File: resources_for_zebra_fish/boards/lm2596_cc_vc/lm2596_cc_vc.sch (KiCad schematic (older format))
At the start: 26 parts, among them J1 Vin, J2 Conn_Coaxial, J3 external_on/off, J4 to_mosfet, J5 red_vout, U1 LM2596T-3.3, U2 LM2596T-ADJ, U3 MCP602

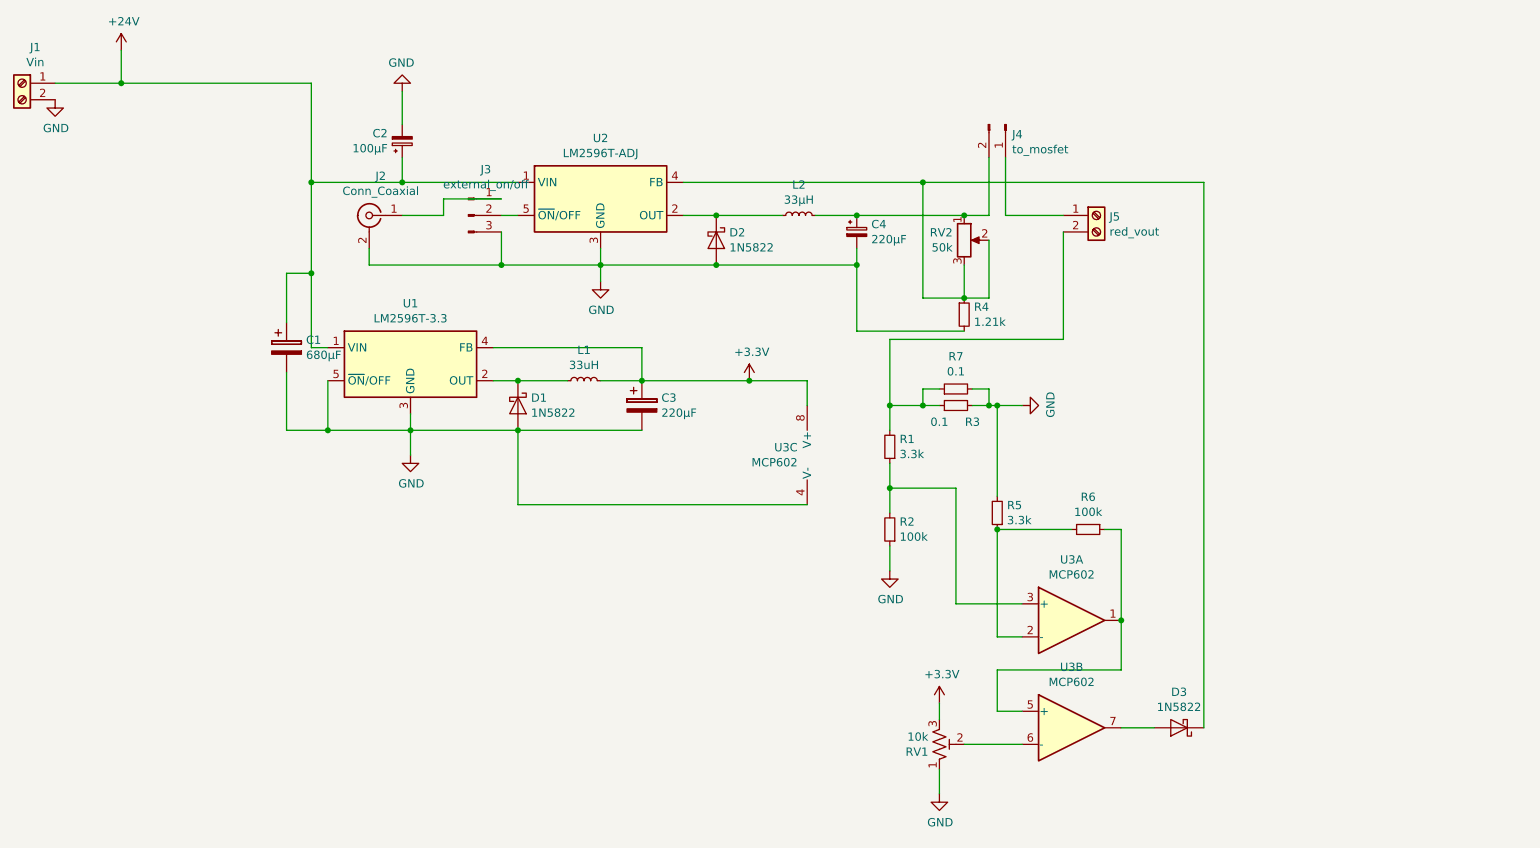
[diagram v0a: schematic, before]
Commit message: new board: power supply and sync to led in one
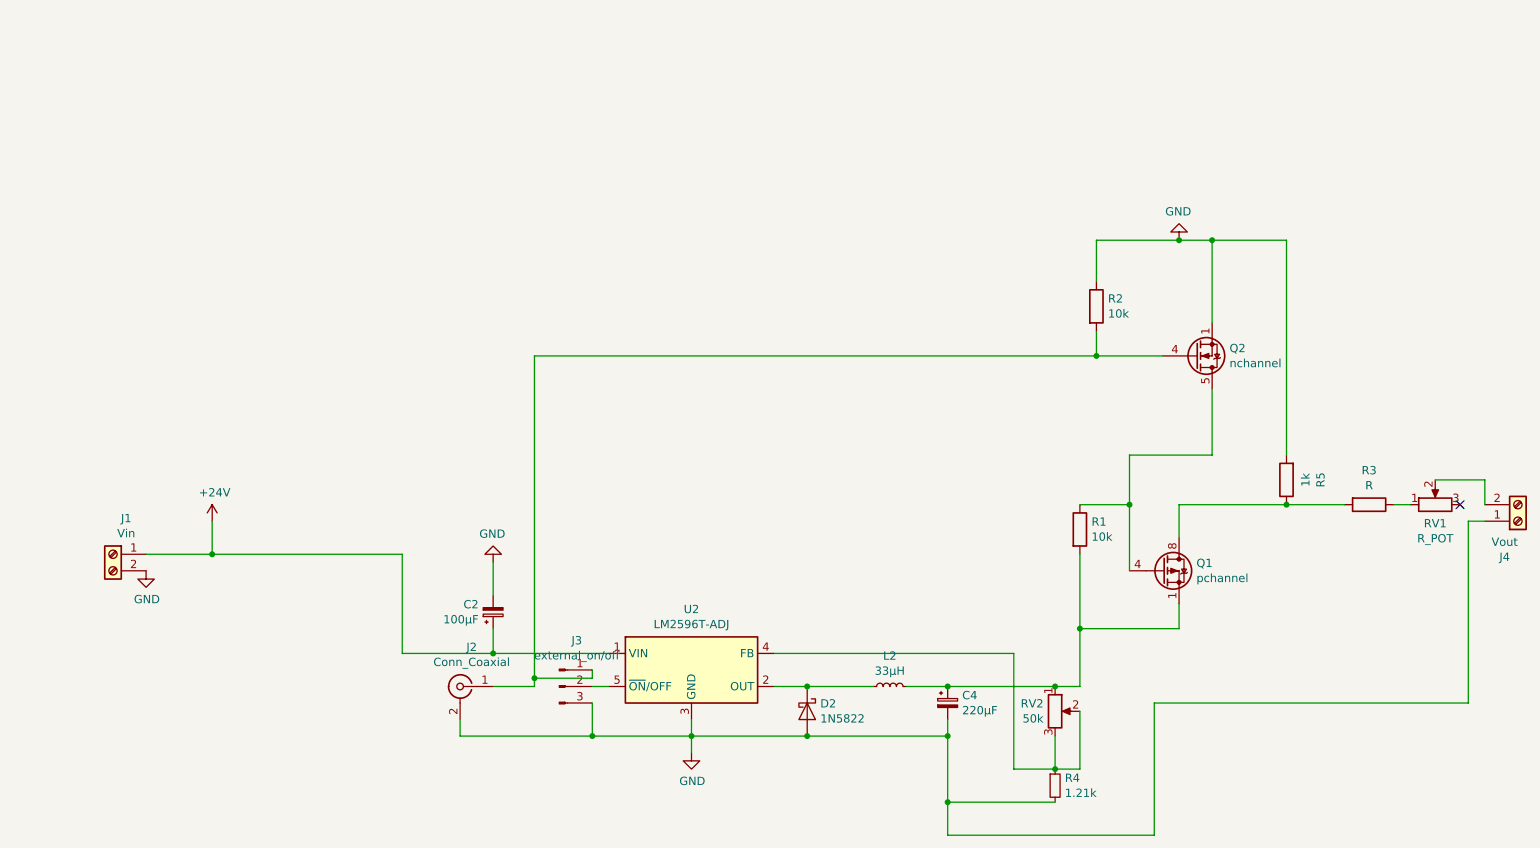
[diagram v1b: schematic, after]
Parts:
- removed C1: 680µF, Capacitor_THT:CP_Radial_D10.0mm_P2.50mm_P5.00mm, symbol Device:CP
- removed C3: 220µF, Capacitor_THT:CP_Radial_D10.0mm_P2.50mm_P5.00mm, symbol Device:CP
- removed D1, D3: 1N5822, Diode_THT:D_DO-201AD_P15.24mm_Horizontal, symbol Diode:1N5822
- removed J4: to_mosfet, Connector_PinHeader_2.54mm:PinHeader_1x02_P2.54mm_Vertical, symbol Connector:Conn_01x02_Male
- removed J5: red_vout, TerminalBlock:TerminalBlock_Altech_AK300-2_P5.00mm, symbol Connector:Screw_Terminal_01x02
- removed L1: 33uH, Inductor_THT:L_Radial_D7.5mm_P3.50mm_Fastron_07P, symbol Device:L_Small
- removed R1, R5: 3.3k, Resistor_THT:R_Axial_DIN0207_L6.3mm_D2.5mm_P7.62mm_Horizontal, symbol Device:R_Small
- removed R2, R6: 100k, Resistor_THT:R_Axial_DIN0207_L6.3mm_D2.5mm_P7.62mm_Horizontal, symbol Device:R_Small
- removed R3, R7: 0.1, Resistor_THT:R_Box_L8.4mm_W2.5mm_P5.08mm, symbol Device:R_Small
- removed RV1: 10k, Potentiometer_THT:Potentiometer_Piher_PT-15-H25_Horizontal, symbol Device:R_POT_TRIM_US
- removed U1: LM2596T-3.3, Package_TO_SOT_THT:TO-220-5_P3.4x3.7mm_StaggerOdd_Lead3.8mm_Vertical, symbol Regulator_Switching:LM2596T-3.3
- removed U3: MCP602, Package_DIP:DIP-8_W7.62mm, symbol Amplifier_Operational:MCP602
- added J4: Vout, TerminalBlock:TerminalBlock_Altech_AK300-2_P5.00mm, symbol Connector:Screw_Terminal_01x02
- added Q1: pchannel, Package_SO:SOIC-8_3.9x4.9mm_P1.27mm, symbol Transistor_FET:IRF7404
- added Q2: nchannel, Package_TO_SOT_SMD:TDSON-8-1, symbol Transistor_FET:CSD17577Q5A
- added R1, R2: 10k, Resistor_THT:R_Axial_DIN0309_L9.0mm_D3.2mm_P12.70mm_Horizontal, symbol Device:R
- added R3: R, Resistor_THT:R_Axial_DIN0309_L9.0mm_D3.2mm_P12.70mm_Horizontal, symbol Device:R
- added R5: 1k, Resistor_THT:R_Axial_DIN0309_L9.0mm_D3.2mm_P12.70mm_Horizontal, symbol Device:R
- added RV1: R_POT, Potentiometer_THT:Potentiometer_Piher_PT-15-H25_Horizontal, symbol Device:R_POT
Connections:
- net GND: now also J4.1 (Pin_1), Q2.1 (S), Q2.2 (S), Q2.3 (S), R2.1, R5.2
- net at C4.1, L2.2, RV2.1: now also Q1.1 (S), Q1.2 (S), Q1.3 (S), R1.2
- net at J2.1 (In), J3.1 (Pin_1): now also Q2.4 (G), R2.2
- new net: Q1.4 (G), Q2.5 (D), R1.1
- new net: Q1.5 (D), Q1.6 (D), Q1.7 (D), Q1.8 (D), R3.2, R5.1
- new net: R3.1, RV1.1
- new net: J4.2 (Pin_2), RV1.2
- no-connect marks 0 -> 1
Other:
- moved on the sheet: C2, C4, D2, J1, J2, J3, L2, R4, RV2, U2
